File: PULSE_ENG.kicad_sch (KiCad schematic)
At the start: 0 parts

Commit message: add pdu libery
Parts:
- added IC1, IC2: INA226AIDGSR, PULSE_Library:SOP50P490X110-10N, symbol PULSE_Library:INA226AIDGSR

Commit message: added schematics hirarchie
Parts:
- removed IC1, IC2: INA226AIDGSR, PULSE_Library:SOP50P490X110-10N, symbol PULSE_Library:INA226AIDGSR
- added H1, H2: ESQ-126-39-G-D, PULSE_Libary:ESQ-126-Y-X-D, symbol EPS_Library:ESQ-126-39-G-D
- added J2, J3, J4, J6: G125-FV10805F3-1AB1ABP, G125-FV10805F3-1AB1ABP (1):HARWIN_G125-FV10805F3-1AB1ABP, symbol G125-FV10805F3-1AB1ABP:G125-FV10805F3-1AB1ABP
- added J7: 12401832E402A, 12401832E402A, symbol 12401832E402A:12401832E402A
- added MH1, MH2, MH3, MH4: MountingHole, MountingHole:MountingHole_3.2mm_M3, symbol Mechanical:MountingHole
- added U1: ATSAMD21J17D-M, Package_DFN_QFN:QFN-64-1EP_9x9mm_P0.5mm_EP4.7x4.7mm, symbol MCU_Microchip_SAMD:ATSAMD21J17D-M
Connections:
- new net 12V_1: H2.43
- new net 12V_2: H2.44
- new net 3V3_1: H1.48
- new net 5V_1: H2.25
- new net 5V_2: H2.26
- new net 5V_BU: H1.47
- new net BU_Vbat_ON: H1.14
- new net GND: H2.29, H2.30, H2.31, H2.32, U1.22 (GND), U1.33 (GND), U1.47 (GND), U1.54 (GND)
- new net GNDANA: U1.7 (GNDANA)
- new net Main_Bus: H1.17
- new net PV1+: J2.A
- new net PV1-: J4.B
- new net PV1_mid: J2.B, J4.A
- new net PV2+: J3.A
- new net PV2-: J6.B
- new net PV2_mid: J3.B, J6.A
- new net RS422_A: H1.29
- new net RS422_B: H1.30
- new net RS422_Y: H1.32
- new net RS422_Z: H1.31
- new net SA_Deploy: H2.23
- new net SA_Deploy_BU: H2.24
- new net UART1_RX: H1.40
- new net UART1_TX: H1.39
- new net UHF_Deploy: H2.28
- new net VDDANA: U1.8 (VDDANA)
- new net VDDCORE: U1.55 (VDDCORE)
- new net VDDIN: U1.56 (VDDIN)
- new net VDDIO: U1.21 (VDDIO)
- new net Vbat_ON: H1.16
- new net Vout1_PMU: H1.20
- new net Vout2_PMU: H1.19
- no-connect marks 0 -> 140
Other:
- added sheet EPS_Power_Supply (EPS_power_supply.kicad_sch)
- added sheet PCU (PCU.kicad_sch)
- added sheet PDU (EPS_PDU.kicad_sch)
- note added: "H1 & H2"
- note added: "Pico-lock header"
- note added: "USB C"
- note added: "needs to by added to pulse libary"
- company: (none) -> EPFL Spacecraft Team
- title: (none) -> PULSE - EPS

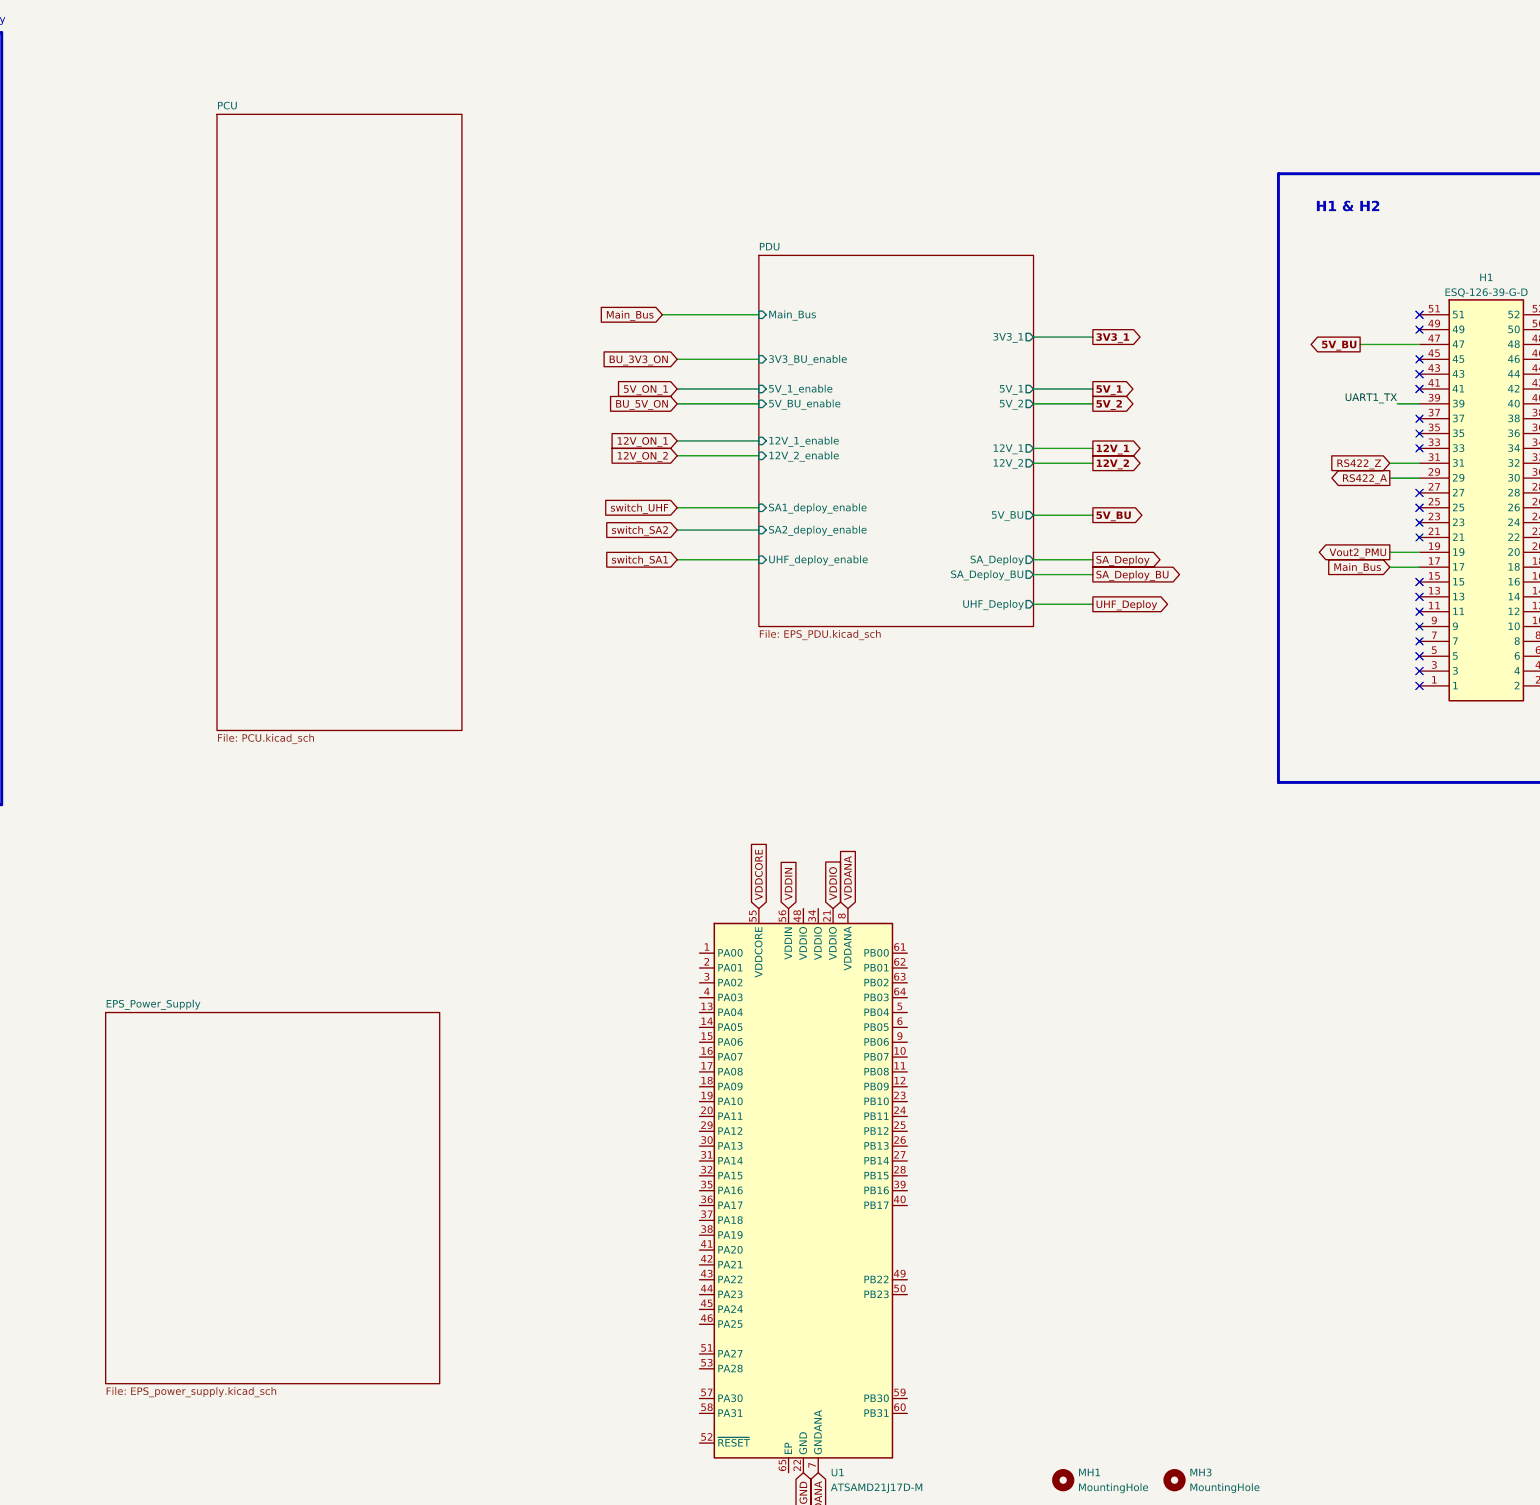
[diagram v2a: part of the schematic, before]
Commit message: changed epc gan symbol
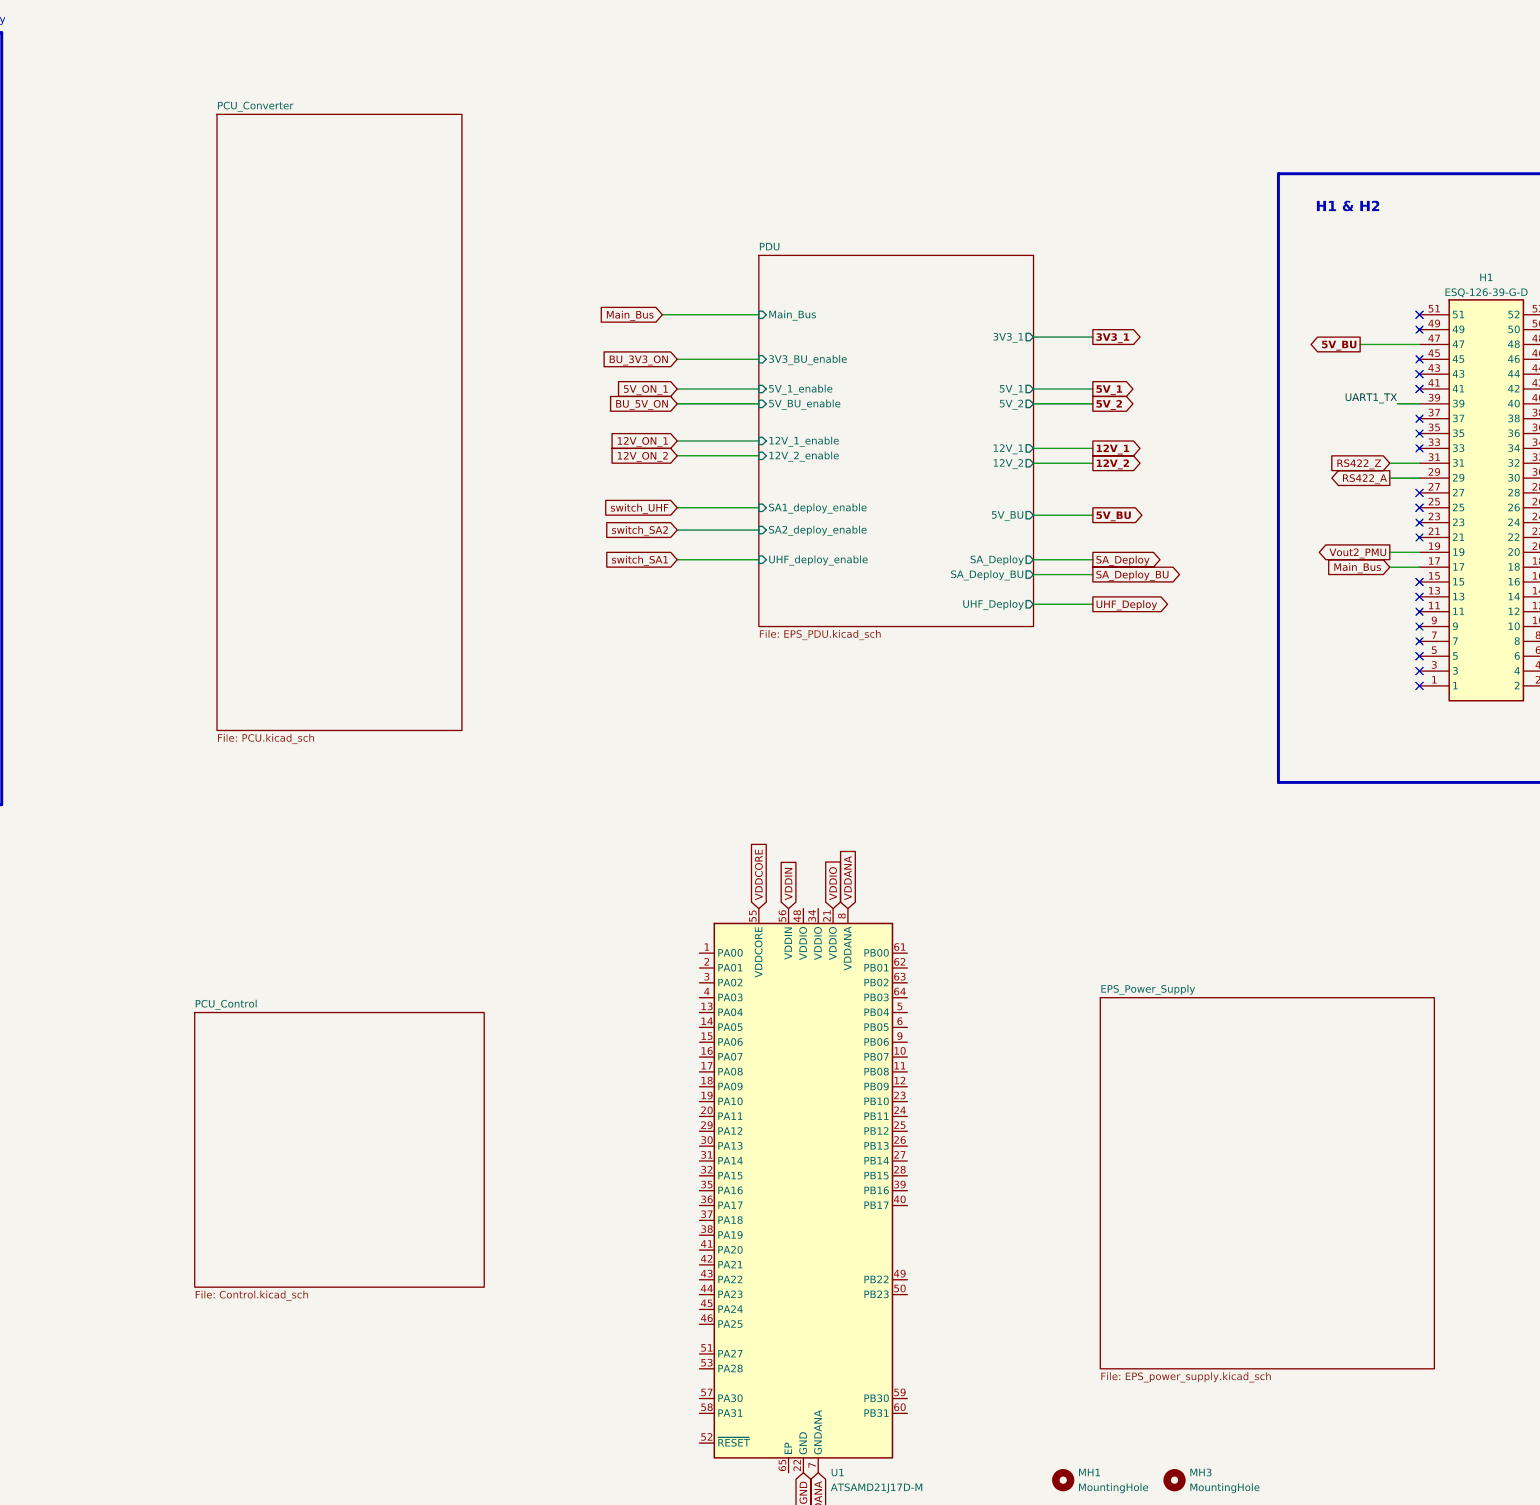
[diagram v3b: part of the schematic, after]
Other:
- sheet PCU renamed PCU_Converter
- added sheet PCU_Control (Control.kicad_sch)
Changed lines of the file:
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@@
 			(color 0 0 0 0.0000)
 		)
-		(property "Sheetname" "PCU"
+		(property "Sheetname" "PCU_Converter"
 			(at 95.25 32.3084 0)
 			(effects
@@
 	)
 	(sheet
-		(at 76.2 186.69)
+		(at 246.38 184.15)
 		(size 57.15 63.5)
 		(exclude_from_sim no)
@@
 		)
 		(property "Sheetname" "EPS_Power_Supply"
-			(at 76.2 185.9784 0)
+			(at 246.38 183.4384 0)
 			(effects
 				(font
@@
 		)
 		(property "Sheetfile" "EPS_power_supply.kicad_sch"
-			(at 76.2 250.7746 0)
+			(at 246.38 248.2346 0)
 			(effects
 				(font
@@
 				)
 			)
+		)
+	)
+	(sheet
+		(at 91.44 186.69)
+		(size 49.53 46.99)
+		(exclude_from_sim no)
+		(in_bom yes)
+		(on_board yes)
+		(dnp no)
+		(fields_autoplaced yes)
+		(stroke
+			(width 0.1524)
+			(type solid)
+		)
+		(fill
+			(color 0 0 0 0.0000)
+		)
+		(property "Sheetname" "PCU_Control"
+			(at 91.44 185.9784 0)
+			(effects
+				(font
+					(size 1.27 1.27)
+				)
+				(justify left bottom)
+			)
+		)
+		(property "Sheetfile" "Control.kicad_sch"
+			(at 91.44 234.2646 0)
+			(effects
+				(font
+					(size 1.27 1.27)
+				)
+				(justify left top)
+			)
+		)
+		(instances
+			(project "PULSE_ENG"
+				(path "/2de881bb-2e2a-47f9-96ed-b3393fa36b98"
+					(page "5")
+				)
+			)

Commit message: Power supply
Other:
- sheet EPS_Power_Supply ports: added 3V3, 3V3_PDU, 5V, 5V_PDU, GND, GNDANA, PV_in, VDDANA, VDDCORE, VDDIN, VDDIO; removed none
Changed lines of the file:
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@@
 	(wire
 		(pts
+			(xy 241.3 224.79) (xy 242.57 224.79)
+		)
+		(stroke
+			(width 0)
+			(type default)
+		)
+	)
+	(wire
+		(pts
 			(xy 353.06 92.71) (xy 353.06 93.98)
 		)
@@
 		)
 	)
+	(global_label "GND"
+		(shape input)
+		(at 241.3 224.79 180)
+		(fields_autoplaced yes)
+		(effects
+			(font
+				(size 1.27 1.27)
+			)
+			(justify right)
+		)
+		(property "Intersheetrefs" "${INTERSHEET_REFS}"
+			(at 234.4443 224.79 0)
+			(effects
+				(font
+					(size 1.27 1.27)
+				)
+				(justify right)
+				(hide yes)
+			)
+		)
+	)
 	(global_label "switch_SA1"
 		(shape input)
@@
 	)
 	(sheet
-		(at 246.38 184.15)
+		(at 242.57 176.53)
 		(size 57.15 63.5)
 		(exclude_from_sim no)
@@
 		)
 		(property "Sheetname" "EPS_Power_Supply"
-			(at 246.38 183.4384 0)
+			(at 242.57 175.8184 0)
 			(effects
 				(font
@@
 		)
 		(property "Sheetfile" "EPS_power_supply.kicad_sch"
-			(at 246.38 248.2346 0)
+			(at 242.57 240.6146 0)
 			(effects
 				(font
@@
 			)
 		)
+		(pin "3V3" output
+			(at 299.72 191.77 0)
+			(effects
+				(font
+					(size 1.27 1.27)
+				)
+				(justify right)
+			)
+		)
+		(pin "5V" output
+			(at 299.72 184.15 0)
+			(effects
+				(font
+					(size 1.27 1.27)
+				)
+				(justify right)
+			)
+		)
+		(pin "GND" input
+			(at 242.57 224.79 180)
+			(effects
+				(font
+					(size 1.27 1.27)
+				)
+				(justify left)
+			)
+		)
+		(pin "PV_in" input
+			(at 242.57 184.15 180)
+			(effects
+				(font
+					(size 1.27 1.27)
+				)
+				(justify left)
+			)
+		)
+		(pin "VDDCORE" output
+			(at 299.72 199.39 0)
+			(effects
+				(font
+					(size 1.27 1.27)
+				)
+				(justify right)
+			)
+		)
+		(pin "VDDIO" output
+			(at 299.72 201.93 0)
+			(effects
+				(font
+					(size 1.27 1.27)
+				)
+				(justify right)
+			)
+		)
+		(pin "VDDIN" output
+			(at 299.72 204.47 0)
+			(effects
+				(font
+					(size 1.27 1.27)
+				)
+				(justify right)
+			)
+		)
+		(pin "VDDANA" output
+			(at 299.72 207.01 0)
+			(effects
+				(font
+					(size 1.27 1.27)
+				)
+				(justify right)
+			)
+		)
+		(pin "GNDANA" output
+			(at 299.72 212.09 0)
+			(effects
+				(font
+					(size 1.27 1.27)
+				)
+				(justify right)
+			)
+		)
+		(pin "5V_PDU" input
+			(at 242.57 191.77 180)
+			(effects
+				(font
+					(size 1.27 1.27)
+				)
+				(justify left)
+			)
+		)
+		(pin "3V3_PDU" input
+			(at 242.57 196.85 180)
+			(effects
+				(font
+					(size 1.27 1.27)
+				)
+				(justify left)
+			)
+		)
